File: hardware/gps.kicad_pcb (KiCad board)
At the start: 2 copper layers, 40 x 35 mm, 33 parts, among them P101 CON-SENSOR, P103 Boot, P104 U.FL, U101 XMC1XXX24, U102 FireFlyX1, U103 DRILL, U104 DRILL, U105 DRILL, U106 DRILL

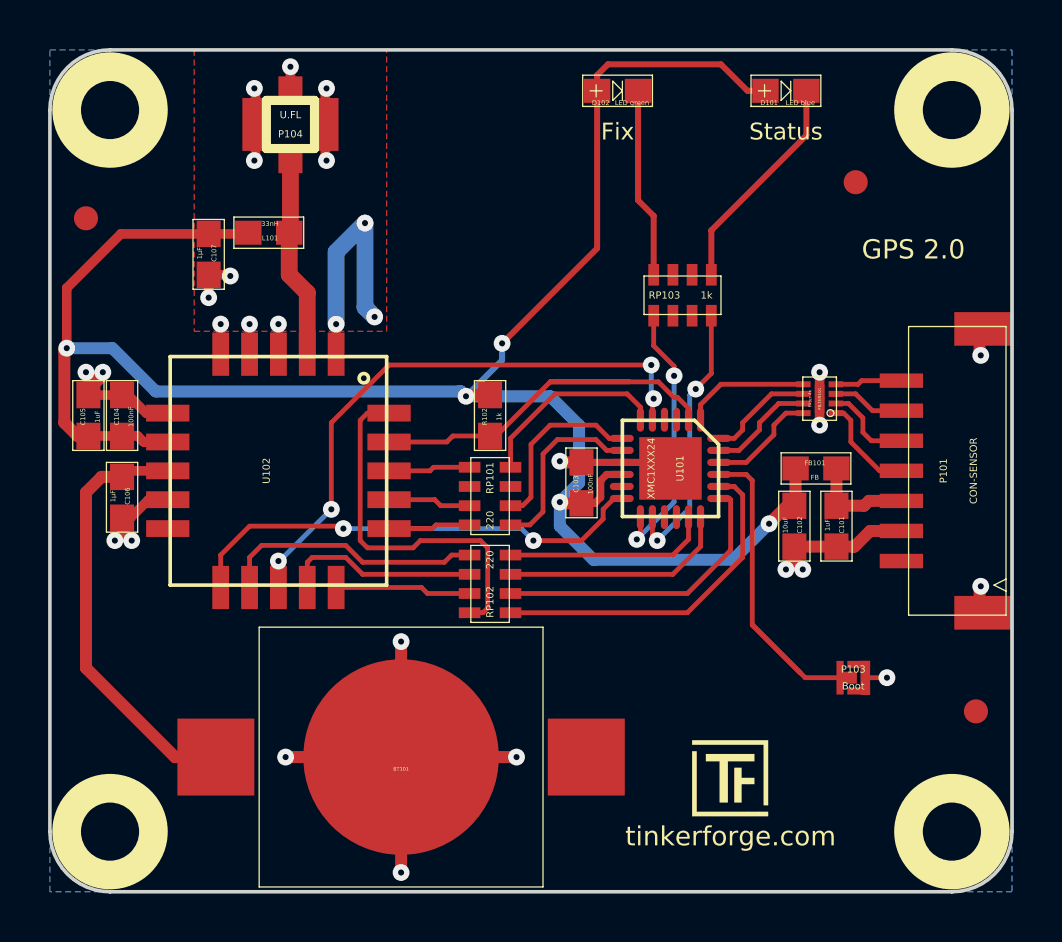
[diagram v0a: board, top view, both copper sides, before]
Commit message: change via size, add spi pulldowns for inputs
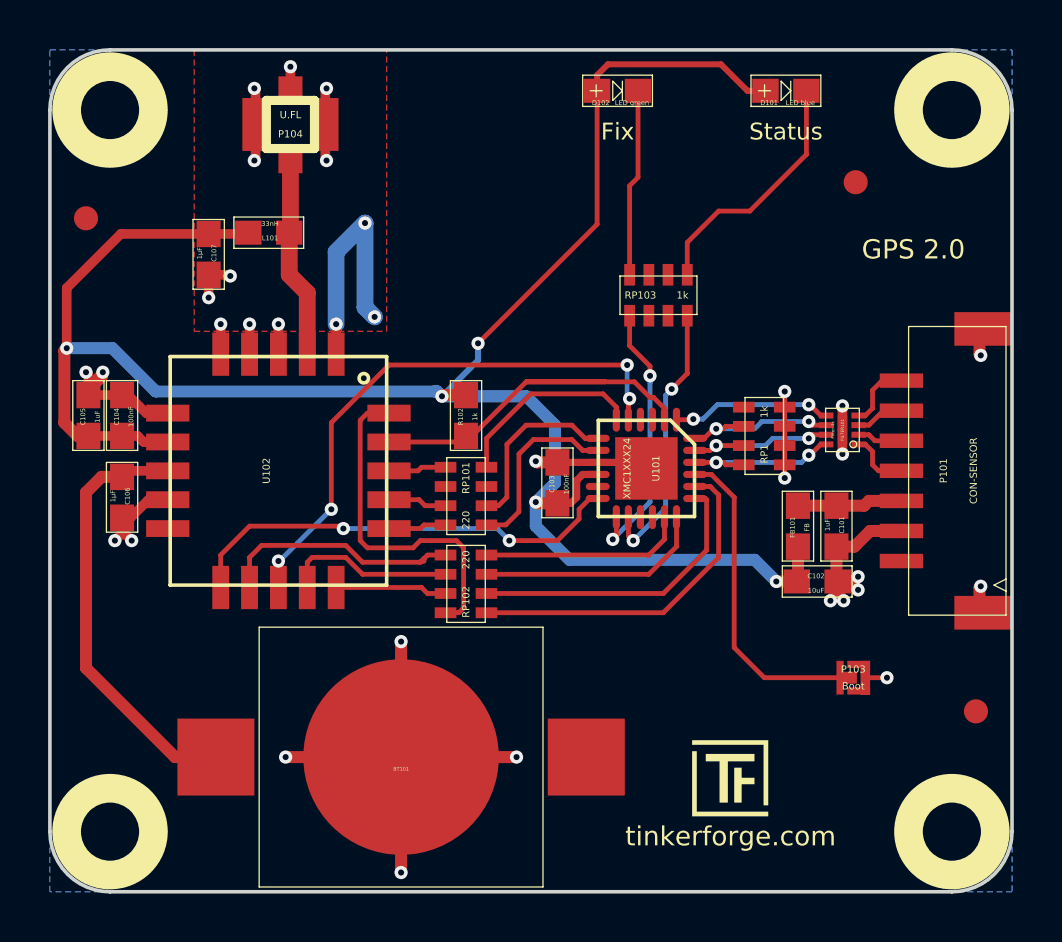
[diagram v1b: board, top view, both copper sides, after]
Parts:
- added RP1: 1k, 0603X4, F.Cu at (196.1, 102.0)
- moved FB101 2.51 mm to (197.5, 105.7), turned to 270 degrees
- moved C102 2.49 mm to (198.3, 108.0), turned to 180 degrees
- moved FILTER101 1.61 mm to (199.3, 101.7)
- moved C103 1.00 mm to (187.5, 103.9)
- moved G*** 1.00 mm to (185.4, 103.4)
- moved R102 1.00 mm to (183.7, 101.1)
- moved RP101 1.00 mm to (183.7, 104.5)
- moved RP102 1.00 mm to (183.7, 108.1)
- moved RP103 1.00 mm to (191.7, 96.1)
- moved U101 1.00 mm to (191.2, 103.3)
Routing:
- net GND: track 74.5 -> 79.8 mm, vias 29 -> 33
- net S-MOSI: track 4.44 -> 6.99 mm, vias 0 -> 2
- net S-CLK: track 4.48 -> 6.87 mm, vias 0 -> 2
- net S-CS: track 4.58 -> 6.95 mm, vias 0 -> 2
- net Net-(FILTER101-Pad2): track 3.72 -> 1.88 mm
- net Net-(FILTER101-Pad1): track 4.25 -> 2.55 mm
- net Net-(P103-Pad2): track 15.3 -> 13.6 mm
- net S-MISO: track 5.25 -> 6.67 mm, vias 0 -> 2
- net Net-(D101-Pad2): track 9.29 -> 10.5 mm
- net Net-(RP101-Pad7): track 3.45 -> 2.45 mm
- net INT: track 24.4 -> 23.4 mm
- net RTCM: track 20.1 -> 19.1 mm
- net RESET: track 17.7 -> 16.7 mm
- net Net-(RP102-Pad4): track 15.3 -> 14.3 mm
- net Net-(RP102-Pad3): track 5.65 -> 4.65 mm
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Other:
- net class Default: trace_width 0.25 -> 0.2; via_dia 0.7 -> 0.55

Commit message: ange serial resistor values
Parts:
- RP101, RP102: value 220 -> 270
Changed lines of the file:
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@@
     (thickness 1.6)
     (drawings 12)
-    (tracks 401)
+    (tracks 398)
     (zones 0)
     (modules 34)
@@
       (effects (font (size 0.29972 0.29972) (thickness 0.0762)))
     )
-    (fp_text value 220 (at 1.00076 0 90) (layer F.SilkS)
-      (effects (font (size 0.29972 0.29972) (thickness 0.0762)))
+    (fp_text value 270 (at 1.00076 0 90) (layer F.SilkS)
+      (effects (font (size 0.29972 0.29972) (thickness 0.07493)))
     )
     (fp_line (start -1.6002 -0.8001) (end 1.6002 -0.8001) (layer F.SilkS) (width 0.001))
@@
       (effects (font (size 0.29972 0.29972) (thickness 0.0762)))
     )
-    (fp_text value 220 (at 1.00076 0 270) (layer F.SilkS)
-      (effects (font (size 0.29972 0.29972) (thickness 0.0762)))
+    (fp_text value 270 (at 1.00076 0 270) (layer F.SilkS)
+      (effects (font (size 0.29972 0.29972) (thickness 0.07493)))
     )
     (fp_line (start -1.6002 -0.8001) (end 1.6002 -0.8001) (layer F.SilkS) (width 0.001))
@@
   (segment (start 174.7 107) (end 174.7 108.25) (width 0.2) (layer F.Cu) (net 29))
   (segment (start 179.4 107.2) (end 178.7 106.5) (width 0.2) (layer F.Cu) (net 29))
-  (segment (start 181.8 107.2) (end 181.85 107.15) (width 0.2) (layer F.Cu) (net 29))
-  (segment (start 181.85 107.15) (end 181.95 107.15) (width 0.2) (layer F.Cu) (net 29))
-  (segment (start 181.95 107.15) (end 181.95 107.05) (width 0.2) (layer F.Cu) (net 29))
   (segment (start 182.8491 106.90112) (end 182.09888 106.90112) (width 0.2) (layer F.Cu) (net 29))
   (segment (start 182.09888 106.90112) (end 181.95 107.05) (width 0.2) (layer F.Cu) (net 29))

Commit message: slot for external antenna added
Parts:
- moved G*** 16.6 mm to (170.1, 97.0)
- moved VAL 12.9 mm to (177.9, 90.5)
- moved VAL 12.9 mm to (194.9, 90.5)
- moved D102 2.00 mm to (192.0, 87.6)
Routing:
- net VCC: track 86.6 -> 91.0 mm
- net Net-(D102-Pad2): track 7.79 -> 8.62 mm
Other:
- outline, holes or cut-outs redrawn
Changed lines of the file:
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@@
     (area 165.544999 85.044999 207.255001 121.755001)
     (thickness 1.6)
-    (drawings 12)
-    (tracks 398)
+    (drawings 24)
+    (tracks 401)
     (zones 0)
     (modules 34)
@@
   )
   (module kicad-libraries:CE_5mm (layer B.Cu)
-    (at 177.9 103.4 180)
+    (at 177.9 90.5 180)
     (fp_text reference VAL (at 0 0 180) (layer B.SilkS) hide
       (effects (font (size 1.143 1.143) (thickness 0.1778)) (justify mirror))
@@
   )
   (module kicad-libraries:WEEE_7mm_back (layer B.Cu)
-    (at 194.9 103.4)
+    (at 194.9 90.5)
     (fp_text reference VAL (at 0 0) (layer B.SilkS) hide
       (effects (font (size 1.143 1.143) (thickness 0.1778)) (justify mirror))
@@
   )
   (module kicad-libraries:D0603E (layer F.Cu)
-    (at 190 87.6)
+    (at 192 87.6)
     (attr smd)
     (fp_text reference D102 (at -0.7 0.5) (layer F.SilkS)
@@
   )
   (module kicad-libraries:Logo_CoMCU (layer B.Cu)
-    (at 185.4 103.4 180)
+    (at 170.1 97 180)
     (fp_text reference G*** (at 0 0 180) (layer B.SilkS) hide
       (effects (font (thickness 0.3)) (justify mirror))
@@
       (net 1 GND))
   )
-  (gr_text Fix (at 190 89.3) (layer F.SilkS)
+  (gr_line (start 188 89.9) (end 184.8 89.9) (angle 90) (layer Edge.Cuts) (width 0.15))
+  (gr_line (start 184.8 87.4) (end 188 87.4) (angle 90) (layer Edge.Cuts) (width 0.15))
+  (gr_line (start 184.4 89.5) (end 184.4 87.8) (angle 90) (layer Edge.Cuts) (width 0.15))
+  (gr_line (start 188.4 89.5) (end 188.4 87.8) (angle 90) (layer Edge.Cuts) (width 0.15))
+  (gr_arc (start 184.8 89.5) (end 184.8 89.9) (angle 90) (layer Edge.Cuts) (width 0.15))
+  (gr_arc (start 188 89.5) (end 188.4 89.5) (angle 90) (layer Edge.Cuts) (width 0.15))
+  (gr_arc (start 188 87.8) (end 188 87.4) (angle 90) (layer Edge.Cuts) (width 0.15))
+  (gr_arc (start 184.8 87.8) (end 184.4 87.8) (angle 90) (layer Edge.Cuts) (width 0.15))
+  (gr_line (start 199.2 95.2) (end 174.2 95.2) (angle 90) (layer B.SilkS) (width 0.2))
+  (gr_line (start 199.2 120.2) (end 199.2 95.2) (angle 90) (layer B.SilkS) (width 0.2))
+  (gr_line (start 174.2 120.2) (end 199.2 120.2) (angle 90) (layer B.SilkS) (width 0.2))
+  (gr_line (start 174.2 95.2) (end 174.2 120.2) (angle 90) (layer B.SilkS) (width 0.2))
+  (gr_text Fix (at 192 89.3) (layer F.SilkS)
     (effects (font (size 0.7 0.7) (thickness 0.15)))
   )
@@
   (segment (start 171.3 103.4) (end 169.6499 103.4) (width 0.4) (layer F.Cu) (net 2))
   (segment (start 169.6499 103.4) (end 169.4 103.6499) (width 0.4) (layer F.Cu) (net 2))
-  (segment (start 189.1499 87.6) (end 189.1499 93.1501) (width 0.2) (layer F.Cu) (net 3))
+  (segment (start 189.1499 91.2) (end 191.1499 89.2) (width 0.2) (layer F.Cu) (net 3))
+  (segment (start 191.1499 89.2) (end 191.1499 87.6) (width 0.2) (layer F.Cu) (net 3))
+  (segment (start 189.1499 87.6) (end 189.1499 91.2) (width 0.2) (layer F.Cu) (net 3))
+  (segment (start 189.1499 91.2) (end 189.1499 93.1501) (width 0.2) (layer F.Cu) (net 3))
   (segment (start 189.1499 93.1501) (end 184.2 98.1) (width 0.2) (layer F.Cu) (net 3))
   (segment (start 197.4499 108) (end 196.6 108) (width 0.5) (layer F.Cu) (net 3))
@@
   (segment (start 184.2 98.8) (end 184.2 98.1) (width 0.25) (layer B.Cu) (net 3))
   (via (at 184.2 98.1) (size 0.55) (drill 0.25) (layers F.Cu B.Cu) (net 3))
-  (segment (start 196.1499 87.6) (end 195.4 87.6) (width 0.25) (layer F.Cu) (net 3))
-  (segment (start 189.1499 86.9501) (end 189.1499 87.6) (width 0.25) (layer F.Cu) (net 3))
-  (segment (start 189.6 86.5) (end 189.1499 86.9501) (width 0.25) (layer F.Cu) (net 3))
-  (segment (start 194.3 86.5) (end 189.6 86.5) (width 0.25) (layer F.Cu) (net 3))
-  (segment (start 195.4 87.6) (end 194.3 86.5) (width 0.25) (layer F.Cu) (net 3))
+  (segment (start 196.1499 87.6) (end 195.4 87.6) (width 0.2) (layer F.Cu) (net 3))
+  (segment (start 189.1499 86.9501) (end 189.1499 87.6) (width 0.2) (layer F.Cu) (net 3))
+  (segment (start 189.6 86.5) (end 189.1499 86.9501) (width 0.2) (layer F.Cu) (net 3))
+  (segment (start 194.3 86.5) (end 189.6 86.5) (width 0.2) (layer F.Cu) (net 3))
+  (segment (start 195.4 87.6) (end 194.3 86.5) (width 0.2) (layer F.Cu) (net 3))
   (segment (start 187.4 103.9) (end 186.6 104.7) (width 0.5) (layer B.Cu) (net 3))
   (segment (start 186.2 100.3) (end 187.4 101.5) (width 0.5) (layer B.Cu) (net 3))
@@
   (segment (start 183.40112 109.29888) (end 182.8491 109.29888) (width 0.2) (layer F.Cu) (net 32))
   (segment (start 179.6 101) (end 180.5 101) (width 0.2) (layer F.Cu) (net 32))
-  (segment (start 190.8501 87.6) (end 190.8501 91.1999) (width 0.2) (layer F.Cu) (net 33))
-  (segment (start 190.50112 91.54888) (end 190.50112 95.2491) (width 0.2) (layer F.Cu) (net 33))
-  (segment (start 190.8501 91.1999) (end 190.50112 91.54888) (width 0.2) (layer F.Cu) (net 33))
+  (segment (start 192.8501 87.6) (end 192.8501 90.5499) (width 0.2) (layer F.Cu) (net 33))
+  (segment (start 190.50112 92.89888) (end 190.50112 95.2491) (width 0.2) (layer F.Cu) (net 33))
+  (segment (start 192.8501 90.5499) (end 190.50112 92.89888) (width 0.2) (layer F.Cu) (net 33))
   (segment (start 191.35 99.75) (end 191.35 99.45) (width 0.2) (layer B.Cu) (net 34))
   (segment (start 191.35 99.04888) (end 190.50112 98.2) (width 0.2) (layer F.Cu) (net 34))

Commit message: Add 3d information (tbc)
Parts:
- C101, C102, C103, C104, C105, C106, C107, FB101, L101: footprint kicad-libraries:0603E -> kicad-libraries:C0603E
- R102: footprint kicad-libraries:0603E -> kicad-libraries:R0603E
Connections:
- P101 pad 1: (no net) -> Net-(P101-Pad1)
- RP1 pad 1: (no net) -> Net-(RP1-Pad1)
- RP101 pad 3: (no net) -> Net-(RP101-Pad3)
- RP101 pad 6: (no net) -> Net-(RP101-Pad6)
- RP103 pad 2: (no net) -> Net-(RP103-Pad2)
- RP103 pad 3: (no net) -> Net-(RP103-Pad3)
- RP103 pad 6: (no net) -> Net-(RP103-Pad6)
- RP103 pad 7: (no net) -> Net-(RP103-Pad7)
- U101 pad 11: (no net) -> Net-(U101-Pad11)
- U101 pad 15: (no net) -> Net-(U101-Pad15)
- U101 pad 16: (no net) -> Net-(U101-Pad16)
- U101 pad 3: (no net) -> Net-(U101-Pad3)
- U101 pad 4: (no net) -> Net-(U101-Pad4)
- U102 pad 10: (no net) -> Net-(U102-Pad10)

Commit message: Add 3d information (final)
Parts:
- added REF**: FT-GPS-001, kicad-libraries:FT-GPS-001, B.Cu at (186.7, 107.7)
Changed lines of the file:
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@@
     (area 166.324999 85.824999 206.475001 120.975001)
     (thickness 1.6)
-    (drawings 24)
+    (drawings 20)
     (tracks 401)
     (zones 0)
-    (modules 34)
+    (modules 35)
     (nets 50)
   )
@@
     (aux_axis_origin 166.4 85.9)
     (grid_origin 166.4 85.9)
-    (visible_elements FFFF7F7F)
+    (visible_elements FFFFFF7F)
     (pcbplotparams
       (layerselection 0x011f8_80000001)
@@
     )
   )
-  (module kicad-libraries:FireFlyX1 (layer F.Cu)
-    (at 175.9 103.4 270)
-    (fp_text reference U102 (at 0 0.5 270) (layer F.SilkS)
-      (effects (font (size 0.3 0.3) (thickness 0.0712)))
-    )
-    (fp_text value FireFlyX1 (at 0 -0.5 270) (layer F.Fab)
-      (effects (font (size 0.3 0.3) (thickness 0.0712)))
-    )
-    (fp_circle (center -3.85 -3.55) (end -3.725 -3.4) (layer F.SilkS) (width 0.15))
-    (fp_line (start -4.75 -4.5) (end 4.75 -4.5) (layer F.SilkS) (width 0.15))
-    (fp_line (start 4.75 -4.5) (end 4.75 4.5) (layer F.SilkS) (width 0.15))
-    (fp_line (start 4.75 4.5) (end -4.75 4.5) (layer F.SilkS) (width 0.15))
-    (fp_line (start -4.75 4.5) (end -4.75 -4.5) (layer F.SilkS) (width 0.15))
-    (pad 1 smd rect (at -4.85 -2.4 270) (size 1.8 0.7) (layers F.Cu F.Paste F.Mask)
-      (net 1 GND))
-    (pad 2 smd rect (at -4.85 -1.2 270) (size 1.8 0.7) (layers F.Cu F.Paste F.Mask)
-      (net 5 "Net-(L101-Pad2)"))
-    (pad 3 smd rect (at -4.85 0 270) (size 1.8 0.7) (layers F.Cu F.Paste F.Mask)
-      (net 1 GND))
-    (pad 4 smd rect (at -4.85 1.2 270) (size 1.8 0.7) (layers F.Cu F.Paste F.Mask)
-      (net 1 GND))
-    (pad 5 smd rect (at -4.85 2.4 270) (size 1.8 0.7) (layers F.Cu F.Paste F.Mask)
-      (net 1 GND))
-    (pad 6 smd rect (at -2.4 4.6 270) (size 0.7 1.8) (layers F.Cu F.Paste F.Mask)
-      (net 1 GND))
-    (pad 7 smd rect (at -1.2 4.6 270) (size 0.7 1.8) (layers F.Cu F.Paste F.Mask)
-      (net 3 VCC))
-    (pad 8 smd rect (at 0 4.6 270) (size 0.7 1.8) (layers F.Cu F.Paste F.Mask)
-      (net 2 +BATT))
-    (pad 9 smd rect (at 1.2 4.6 270) (size 0.7 1.8) (layers F.Cu F.Paste F.Mask)
-      (net 1 GND))
-    (pad 10 smd rect (at 2.4 4.6 270) (size 0.7 1.8) (layers F.Cu F.Paste F.Mask)
-      (net 49 "Net-(U102-Pad10)"))
-    (pad 11 smd rect (at 4.85 2.4 270) (size 1.8 0.7) (layers F.Cu F.Paste F.Mask)
-      (net 17 RTCM))
-    (pad 12 smd rect (at 4.85 1.2 270) (size 1.8 0.7) (layers F.Cu F.Paste F.Mask)
-      (net 29 "Net-(RP102-Pad1)"))
-    (pad 13 smd rect (at 4.85 0 270) (size 1.8 0.7) (layers F.Cu F.Paste F.Mask)
-      (net 18 INT))
-    (pad 14 smd rect (at 4.85 -1.2 270) (size 1.8 0.7) (layers F.Cu F.Paste F.Mask)
-      (net 30 "Net-(RP102-Pad2)"))
-    (pad 15 smd rect (at 4.85 -2.4 270) (size 1.8 0.7) (layers F.Cu F.Paste F.Mask)
-      (net 31 "Net-(RP102-Pad3)"))
-    (pad 16 smd rect (at 2.4 -4.6 270) (size 0.7 1.8) (layers F.Cu F.Paste F.Mask)
-      (net 16 "Net-(RP101-Pad8)"))
-    (pad 17 smd rect (at 1.2 -4.6 270) (size 0.7 1.8) (layers F.Cu F.Paste F.Mask)
-      (net 15 "Net-(RP101-Pad7)"))
-    (pad 18 smd rect (at 0 -4.6 270) (size 0.7 1.8) (layers F.Cu F.Paste F.Mask)
-      (net 14 "Net-(RP101-Pad5)"))
-    (pad 19 smd rect (at -1.2 -4.6 270) (size 0.7 1.8) (layers F.Cu F.Paste F.Mask)
-      (net 10 RESET))
-    (pad 20 smd rect (at -2.4 -4.6 270) (size 0.7 1.8) (layers F.Cu F.Paste F.Mask)
-      (net 32 "Net-(RP102-Pad4)"))
-  )
   (module kicad-libraries:DRILL_NP (layer F.Cu)
     (at 168.9 118.4)
@@
       (at (xyz 0 0 0))
       (scale (xyz 1 1 1))
-      (rotate (xyz 0 180 0))
+      (rotate (xyz 0 0 0))
+    )
+  )
+  (module kicad-libraries:FireFlyX1 (layer F.Cu)
+    (at 175.9 103.4 270)
+    (fp_text reference U102 (at 0 0.5 270) (layer F.Fab)
+      (effects (font (size 0.3 0.3) (thickness 0.0712)))
+    )
+    (fp_text value FireFlyX1 (at 0 -0.5 270) (layer F.Fab)
+      (effects (font (size 0.3 0.3) (thickness 0.0712)))
+    )
+    (fp_circle (center -3.85 -3.55) (end -3.725 -3.4) (layer F.Fab) (width 0.15))
+    (fp_line (start -4.75 -4.5) (end 4.75 -4.5) (layer F.Fab) (width 0.15))
+    (fp_line (start 4.75 -4.5) (end 4.75 4.5) (layer F.Fab) (width 0.15))
+    (fp_line (start 4.75 4.5) (end -4.75 4.5) (layer F.Fab) (width 0.15))
+    (fp_line (start -4.75 4.5) (end -4.75 -4.5) (layer F.Fab) (width 0.15))
+    (pad 1 smd rect (at -4.85 -2.4 270) (size 1.8 0.7) (layers F.Cu F.Paste F.Mask)
+      (net 1 GND))
+    (pad 2 smd rect (at -4.85 -1.2 270) (size 1.8 0.7) (layers F.Cu F.Paste F.Mask)
+      (net 5 "Net-(L101-Pad2)"))
+    (pad 3 smd rect (at -4.85 0 270) (size 1.8 0.7) (layers F.Cu F.Paste F.Mask)
+      (net 1 GND))
+    (pad 4 smd rect (at -4.85 1.2 270) (size 1.8 0.7) (layers F.Cu F.Paste F.Mask)
+      (net 1 GND))
+    (pad 5 smd rect (at -4.85 2.4 270) (size 1.8 0.7) (layers F.Cu F.Paste F.Mask)
+      (net 1 GND))
+    (pad 6 smd rect (at -2.4 4.6 270) (size 0.7 1.8) (layers F.Cu F.Paste F.Mask)
+      (net 1 GND))
+    (pad 7 smd rect (at -1.2 4.6 270) (size 0.7 1.8) (layers F.Cu F.Paste F.Mask)
+      (net 3 VCC))
+    (pad 8 smd rect (at 0 4.6 270) (size 0.7 1.8) (layers F.Cu F.Paste F.Mask)
+      (net 2 +BATT))
+    (pad 9 smd rect (at 1.2 4.6 270) (size 0.7 1.8) (layers F.Cu F.Paste F.Mask)
+      (net 1 GND))
+    (pad 10 smd rect (at 2.4 4.6 270) (size 0.7 1.8) (layers F.Cu F.Paste F.Mask)
+      (net 49 "Net-(U102-Pad10)"))
+    (pad 11 smd rect (at 4.85 2.4 270) (size 1.8 0.7) (layers F.Cu F.Paste F.Mask)
+      (net 17 RTCM))
+    (pad 12 smd rect (at 4.85 1.2 270) (size 1.8 0.7) (layers F.Cu F.Paste F.Mask)
+      (net 29 "Net-(RP102-Pad1)"))
+    (pad 13 smd rect (at 4.85 0 270) (size 1.8 0.7) (layers F.Cu F.Paste F.Mask)
+      (net 18 INT))
+    (pad 14 smd rect (at 4.85 -1.2 270) (size 1.8 0.7) (layers F.Cu F.Paste F.Mask)
+      (net 30 "Net-(RP102-Pad2)"))
+    (pad 15 smd rect (at 4.85 -2.4 270) (size 1.8 0.7) (layers F.Cu F.Paste F.Mask)
+      (net 31 "Net-(RP102-Pad3)"))
+    (pad 16 smd rect (at 2.4 -4.6 270) (size 0.7 1.8) (layers F.Cu F.Paste F.Mask)
+      (net 16 "Net-(RP101-Pad8)"))
+    (pad 17 smd rect (at 1.2 -4.6 270) (size 0.7 1.8) (layers F.Cu F.Paste F.Mask)
+      (net 15 "Net-(RP101-Pad7)"))
+    (pad 18 smd rect (at 0 -4.6 270) (size 0.7 1.8) (layers F.Cu F.Paste F.Mask)
+      (net 14 "Net-(RP101-Pad5)"))
+    (pad 19 smd rect (at -1.2 -4.6 270) (size 0.7 1.8) (layers F.Cu F.Paste F.Mask)
+      (net 10 RESET))
+    (pad 20 smd rect (at -2.4 -4.6 270) (size 0.7 1.8) (layers F.Cu F.Paste F.Mask)
+      (net 32 "Net-(RP102-Pad4)"))
+    (model unsorted/FireFlyX1.wrl
+      (at (xyz 0 0 0))
+      (scale (xyz 1 1 1))
+      (rotate (xyz 0 0 0))
+    )
+  )
+  (module kicad-libraries:FT-GPS-001 (layer B.Cu)
+    (at 186.7 107.7)
+    (fp_text reference REF** (at 0.4 -1.1) (layer B.Fab)
+      (effects (font (size 1 1) (thickness 0.15)) (justify mirror))
+    )
+    (fp_text value FT-GPS-001 (at 0.4 1.1) (layer B.Fab)
+      (effects (font (size 1 1) (thickness 0.15)) (justify mirror))
+    )
+    (fp_line (start -12.5 12.5) (end 12.5 12.5) (layer B.SilkS) (width 0.15))
+    (fp_line (start 12.5 12.5) (end 12.5 -12.5) (layer B.SilkS) (width 0.15))
+    (fp_line (start 12.5 -12.5) (end -12.5 -12.5) (layer B.SilkS) (width 0.15))
+    (fp_line (start -12.5 -12.5) (end -12.5 12.5) (layer B.SilkS) (width 0.15))
+    (model unsorted/FT-GPS-001.wrl
+      (at (xyz 0 0 0))
+      (scale (xyz 1 1 1))
+      (rotate (xyz 0 0 180))
     )
   )
@@
   (gr_arc (start 188 87.8) (end 188 87.4) (angle 90) (layer Edge.Cuts) (width 0.15))
   (gr_arc (start 184.8 87.8) (end 184.4 87.8) (angle 90) (layer Edge.Cuts) (width 0.15))
-  (gr_line (start 199.2 95.2) (end 174.2 95.2) (angle 90) (layer B.SilkS) (width 0.2))
-  (gr_line (start 199.2 120.2) (end 199.2 95.2) (angle 90) (layer B.SilkS) (width 0.2))
-  (gr_line (start 174.2 120.2) (end 199.2 120.2) (angle 90) (layer B.SilkS) (width 0.2))
-  (gr_line (start 174.2 95.2) (end 174.2 120.2) (angle 90) (layer B.SilkS) (width 0.2))
   (gr_text Fix (at 192 89.3) (layer F.SilkS)
     (effects (font (size 0.7 0.7) (thickness 0.15)))

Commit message: specify processor
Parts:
- U101: value XMC1XXX24 -> XMC1302-32
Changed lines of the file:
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@@
-(kicad_pcb (version 4) (host pcbnew 4.0.2+dfsg1-stable)
+(kicad_pcb (version 4) (host pcbnew 4.0.7-e2-6376~58~ubuntu17.04.1)
   (general
     (links 85)
     (no_connects 1)
-    (area 166.324999 85.824999 206.475001 120.975001)
+    (area 165.544999 85.044999 207.255001 121.755001)
     (thickness 1.6)
     (drawings 20)
@@
   (page A4)
   (layers
-    (0 F.Cu signal)
-    (31 B.Cu signal)
+    (0 F.Cu signal hide)
+    (31 B.Cu signal hide)
     (32 B.Adhes user hide)
     (33 F.Adhes user hide)
@@
       (effects (font (size 0.3 0.3) (thickness 0.075)))
     )
-    (fp_text value XMC1XXX24 (at 0 0.8 270) (layer F.Fab)
+    (fp_text value XMC1302-32 (at 0 0.8 270) (layer F.Fab)
       (effects (font (size 0.3 0.3) (thickness 0.075)))
     )
